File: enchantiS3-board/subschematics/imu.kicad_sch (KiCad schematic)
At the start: 7 parts, among them U3 ICM-42670-P, U8 MMC5983MA

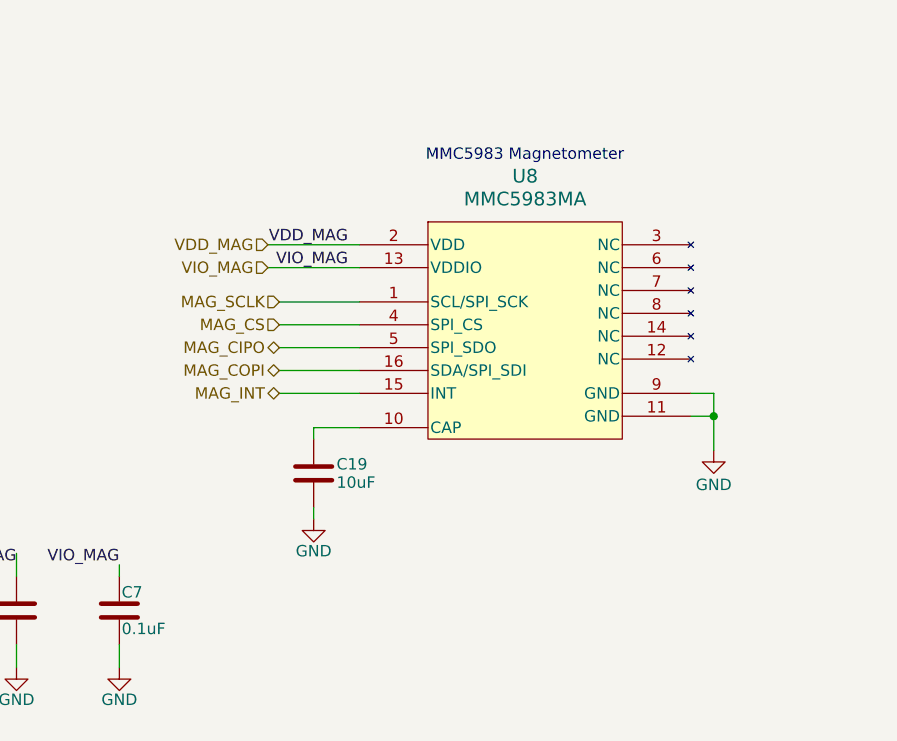
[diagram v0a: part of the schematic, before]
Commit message: Moved all subschematics to a folder
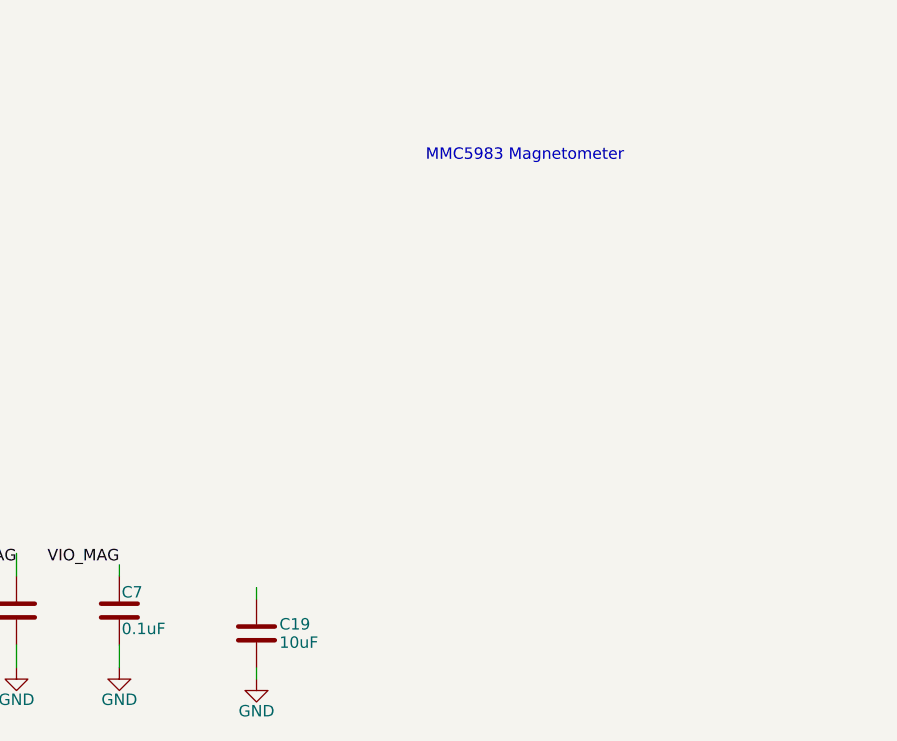
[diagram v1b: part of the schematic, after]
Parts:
- removed U8: MMC5983MA, ENCHANTI_MEMS:MMC5983MA_MEM, symbol ENCHANTI_mems:MMC5983MA

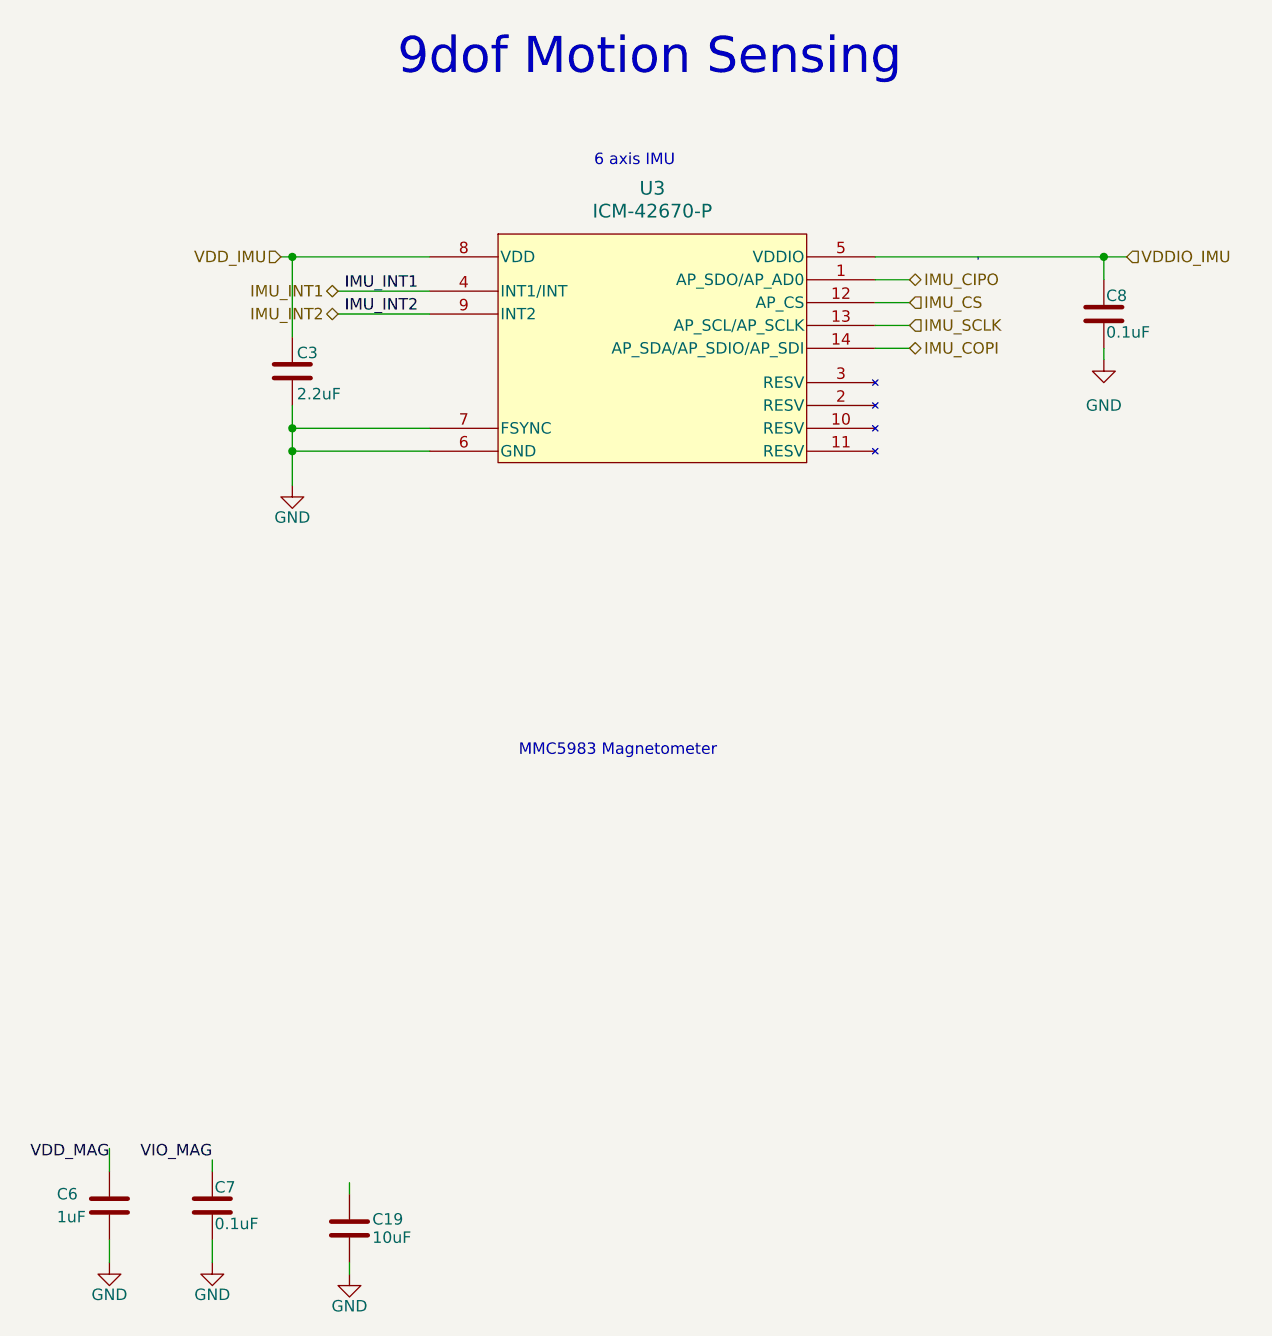
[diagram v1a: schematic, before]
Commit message: Added circuit for magnetometer, added circuit for canfd transceiver, updated circuit for USB connector
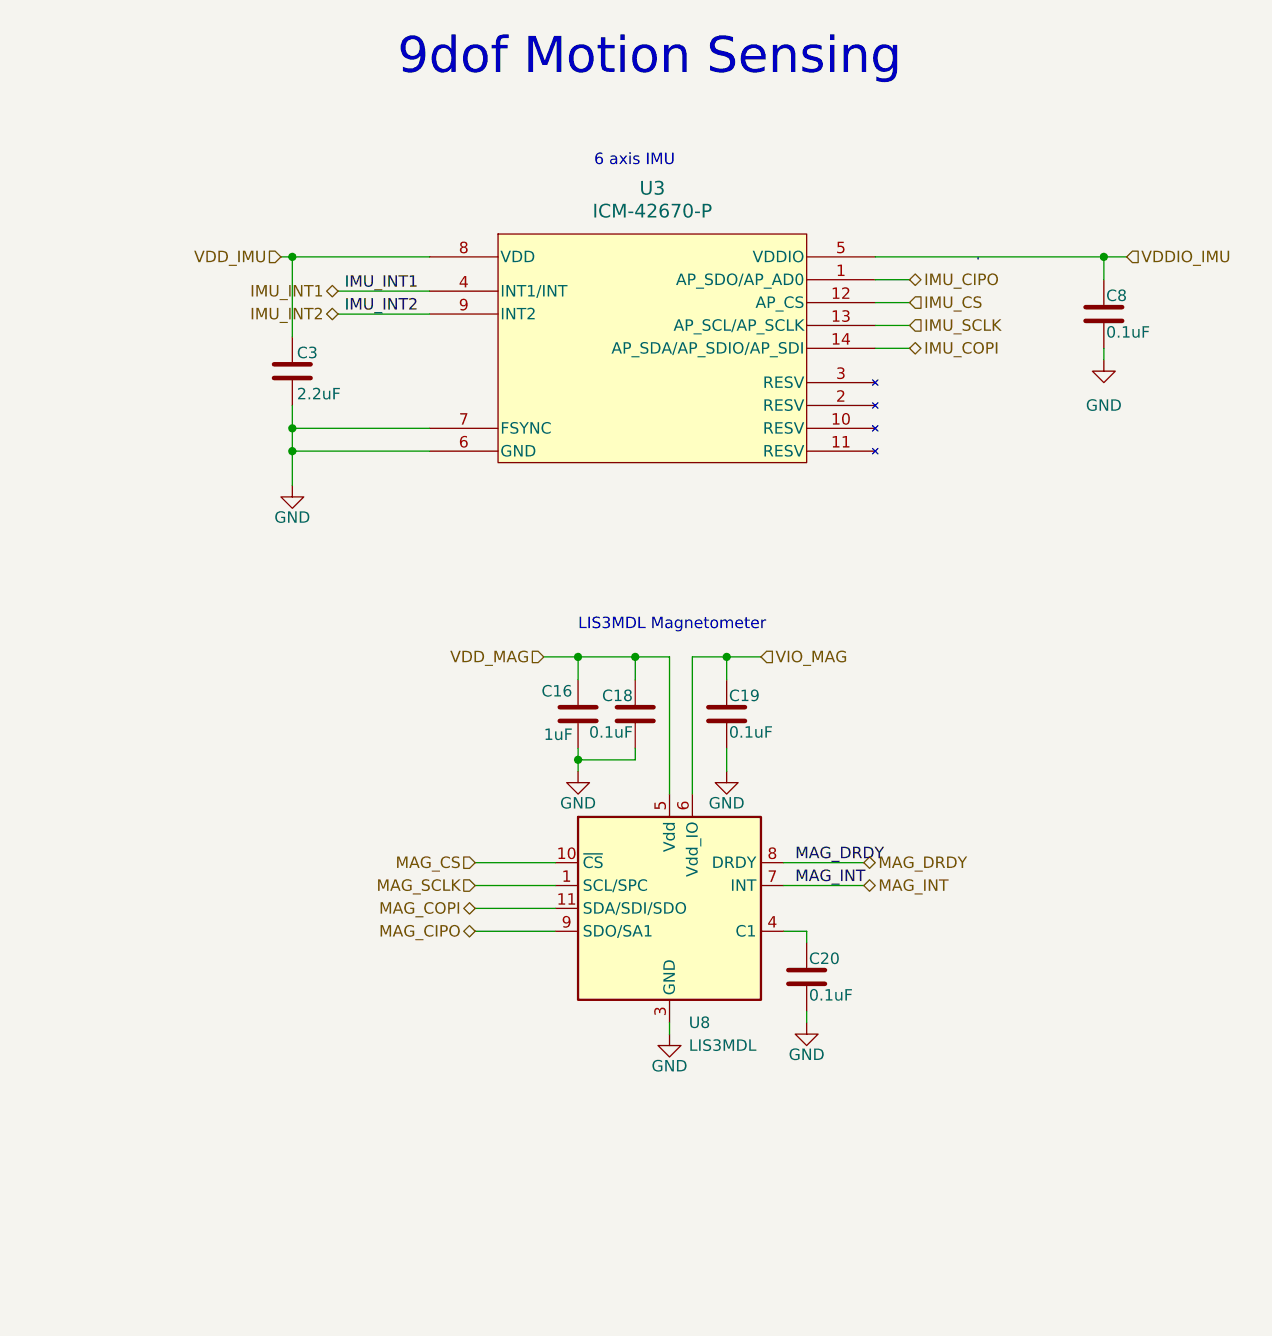
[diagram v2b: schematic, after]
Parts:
- removed C6: 1uF, Capacitor_SMD:C_0402_1005Metric, symbol Device:C
- removed C7: 0.1uF, Capacitor_SMD:C_0402_1005Metric, symbol Device:C
- added C16: 1uF, Capacitor_SMD:C_0402_1005Metric, symbol Device:C
- added C18, C20: 0.1uF, Capacitor_SMD:C_0402_1005Metric, symbol Device:C
- added U8: LIS3MDL, Package_LGA:LGA-12_2x2mm_P0.5mm, symbol Sensor_Magnetic:LIS3MDL
- C19: value 10uF -> 0.1uF; footprint Capacitor_SMD:C_0603_1608Metric -> Capacitor_SMD:C_0402_1005Metric; Mfg Part # GRT188R61C106KE13D -> GRM155R71C104KA88J
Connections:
- net GND: now also C16.2, C18.2, C20.2, U8.12 (GND), U8.2 (GND), U8.3 (GND)
- net VDD_MAG: now also C16.1, C18.1, U8.5 (Vdd)
- net VIO_MAG: now also C19.1, U8.6 (Vdd_IO)
- new net: C20.1, U8.4 (C1)
- new net MAG_CIPO: U8.9 (SDO/SA1)
- new net MAG_COPI: U8.11 (SDA/SDI/SDO)
- new net MAG_CS: U8.10 (~{CS})
- new net MAG_DRDY: U8.8 (DRDY)
- new net MAG_INT: U8.7 (INT)
- new net MAG_SCLK: U8.1 (SCL/SPC)
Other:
- note added: "LIS3MDL Magnetometer"
- note removed: "MMC5983 Magnetometer"

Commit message: Added can transceiver circuit, finished routing power traces
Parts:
- removed C18: 0.1uF, Capacitor_SMD:C_0402_1005Metric, symbol Device:C
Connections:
- net C1: now reaches C20.1, U8.4 (C1)
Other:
- moved on the sheet: C16
